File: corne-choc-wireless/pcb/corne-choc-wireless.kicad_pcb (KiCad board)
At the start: 2 copper layers, 275.5 x 105.6 mm, 118 parts, among them J2 Nice!View, J4 Nice!View, SW1 SW_PUSH, SW10 SW_PUSH, SW11 SW_PUSH, SW12 SW_PUSH, SW13 SW_PUSH, SW14 SW_PUSH, SW15 SW_PUSH, SW16 SW_PUSH, SW17 SW_PUSH, SW18 SW_PUSH, SW19 SW_PUSH, SW2 SW_PUSH, SW20 SW_PUSH, SW21 SW_PUSH, SW22 SW_PUSH, SW23 SW_PUSH, SW24 SW_PUSH, SW25 SW_PUSH, SW26 SW_PUSH, SW27 SW_PUSH, SW29 SW_PUSH, SW3 SW_PUSH, SW30 SW_PUSH, SW31 SW_PUSH, SW32 SW_PUSH, SW33 SW_PUSH, SW34 SW_PUSH, SW35 SW_PUSH, SW36 SW_PUSH, SW37 SW_PUSH, SW38 SW_PUSH, SW39 SW_PUSH, SW4 SW_PUSH, SW40 SW_PUSH, SW41 SW_PUSH, SW42 SW_PUSH, SW5 SW_PUSH, SW6 SW_PUSH, SW8 SW_PUSH, SW9 SW_PUSH, U1 Nice!Nano, U2 Nice!Nano

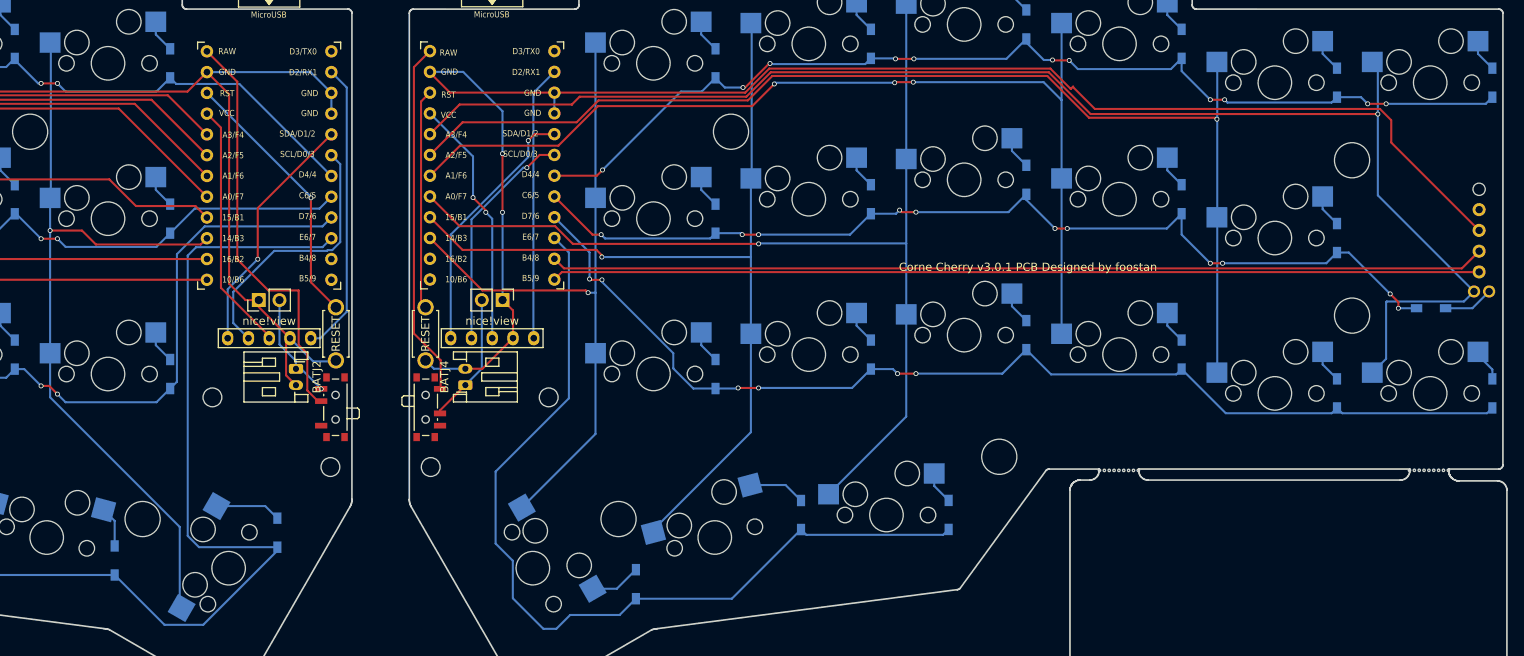
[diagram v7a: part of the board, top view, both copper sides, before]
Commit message: Wide tracks
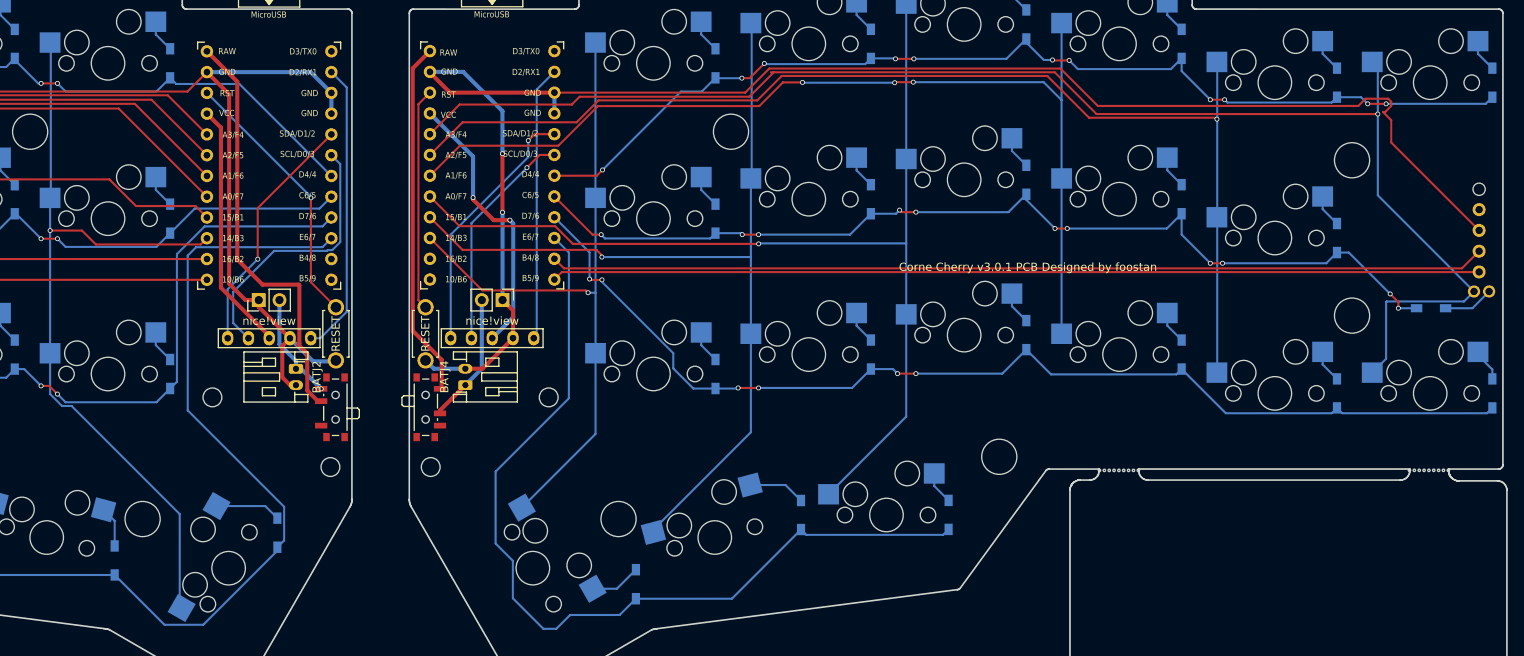
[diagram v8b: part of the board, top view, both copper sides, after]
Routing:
- net row3: track 112.7 -> 107.8 mm
- net VDD: track 30.6 -> 33.9 mm
- net GNDA: track 195.1 -> 197.9 mm
- net row0_r: track 128.7 -> 127.8 mm
- net GND: track 199.5 -> 200.3 mm
- net col5: track 95.5 -> 96.2 mm
